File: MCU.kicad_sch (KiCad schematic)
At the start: 1 part, among them U5 STM32WB55CGUx

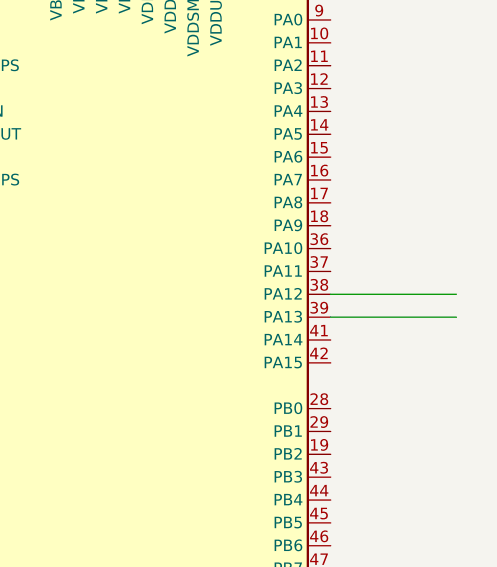
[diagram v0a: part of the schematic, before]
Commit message: added eink conn page
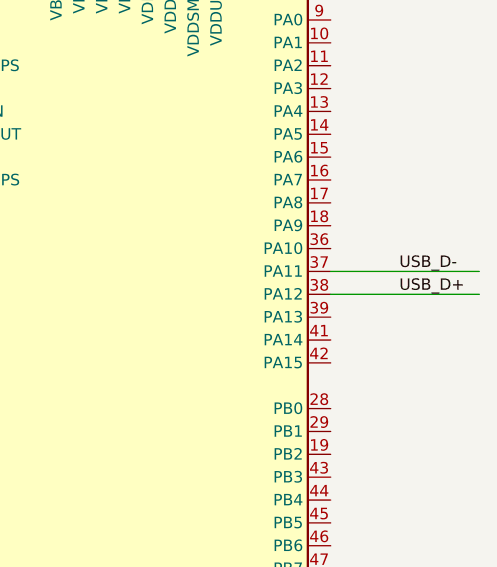
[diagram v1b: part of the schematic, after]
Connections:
- net USB_D-: now reaches U5.37 (PA11)
- net USB_D+: now reaches U5.38 (PA12)
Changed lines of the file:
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@@
+	(wire
+		(pts
+			(xy 168.91 87.63) (xy 185.42 87.63)
+		)
+		(stroke
+			(width 0)
+			(type default)
+		)
+	)
+	(wire
+		(pts
+			(xy 168.91 85.09) (xy 185.42 85.09)
+		)
+		(stroke
+			(width 0)
+			(type default)
+		)
+	)
 	(wire
 		(pts
@@
 	(wire
 		(pts
-			(xy 168.91 87.63) (xy 182.88 87.63)
-		)
-		(stroke
-			(width 0)
-			(type default)
-		)
-	)
-	(wire
-		(pts
 			(xy 146.05 137.16) (xy 146.05 139.7)
 		)
@@
 		)
 	)
-	(wire
-		(pts
-			(xy 168.91 90.17) (xy 182.88 90.17)
+	(label "USB_D-"
+		(at 176.53 85.09 0)
+		(effects
+			(font
+				(size 1.27 1.27)
+			)
+			(justify left bottom)
 		)
-		(stroke
-			(width 0)
-			(type default)
+	)
+	(label "USB_D+"
+		(at 176.53 87.63 0)
+		(effects
+			(font
+				(size 1.27 1.27)
+			)
+			(justify left bottom)
 		)
 	)
@@
 		(on_board yes)
 		(dnp no)
-		(fields_autoplaced yes)
 		(property "Reference" "U5"
 			(at 150.7333 130.81 0)

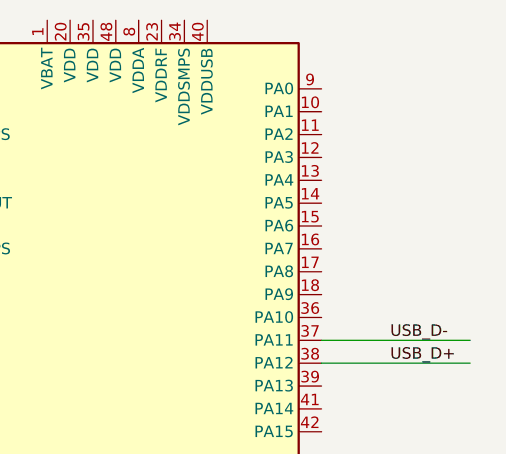
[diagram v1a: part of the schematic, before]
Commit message: eink-> mcu connections
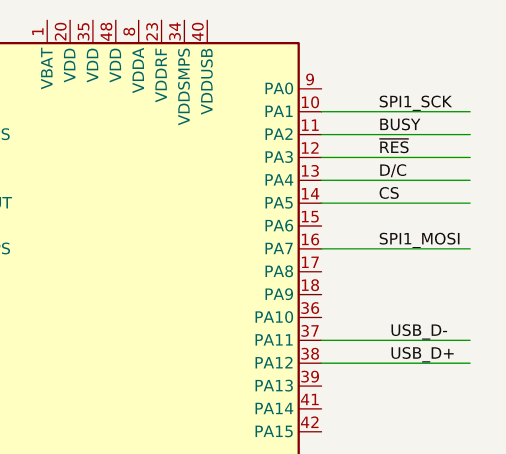
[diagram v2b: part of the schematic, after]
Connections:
- net SPI1_SCK: now reaches U5.10 (PA1)
- net BUSY: now reaches U5.11 (PA2)
- net ~{RES}: now reaches U5.12 (PA3)
- net D/C: now reaches U5.13 (PA4)
- net CS: now reaches U5.14 (PA5)
- net SPI1_MOSI: now reaches U5.16 (PA7)
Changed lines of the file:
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@@
+	(wire
+		(pts
+			(xy 168.91 64.77) (xy 185.42 64.77)
+		)
+		(stroke
+			(width 0)
+			(type default)
+		)
+	)
 	(wire
 		(pts
 			(xy 143.51 137.16) (xy 146.05 137.16)
+		)
+		(stroke
+			(width 0)
+			(type default)
+		)
+	)
+	(wire
+		(pts
+			(xy 168.91 69.85) (xy 185.42 69.85)
 		)
 		(stroke
@@
 	(wire
 		(pts
+			(xy 168.91 67.31) (xy 185.42 67.31)
+		)
+		(stroke
+			(width 0)
+			(type default)
+		)
+	)
+	(wire
+		(pts
 			(xy 143.51 130.81) (xy 143.51 137.16)
 		)
@@
 	(wire
 		(pts
+			(xy 168.91 62.23) (xy 185.42 62.23)
+		)
+		(stroke
+			(width 0)
+			(type default)
+		)
+	)
+	(wire
+		(pts
+			(xy 168.91 59.69) (xy 185.42 59.69)
+		)
+		(stroke
+			(width 0)
+			(type default)
+		)
+	)
+	(wire
+		(pts
 			(xy 146.05 137.16) (xy 148.59 137.16)
+		)
+		(stroke
+			(width 0)
+			(type default)
+		)
+	)
+	(wire
+		(pts
+			(xy 168.91 74.93) (xy 185.42 74.93)
 		)
 		(stroke
@@
 		)
 	)
+	(label "CS"
+		(at 175.26 69.85 0)
+		(effects
+			(font
+				(size 1.27 1.27)
+			)
+			(justify left bottom)
+		)
+	)
+	(label "D{slash}C"
+		(at 175.26 67.31 0)
+		(effects
+			(font
+				(size 1.27 1.27)
+			)
+			(justify left bottom)
+		)
+	)
+	(label "SPI1_MOSI"
+		(at 175.26 74.93 0)
+		(effects
+			(font
+				(size 1.27 1.27)
+			)
+			(justify left bottom)
+		)
+	)
 	(label "USB_D-"
 		(at 176.53 85.09 0)
+		(effects
+			(font
+				(size 1.27 1.27)
+			)
+			(justify left bottom)
+		)
+	)
+	(label "~{RES}"
+		(at 175.26 64.77 0)
 		(effects
 			(font
@@
 		(effects
 			(font
+				(size 1.27 1.27)
+			)
+			(justify left bottom)
+		)
+	)
+	(label "BUSY"
+		(at 175.26 62.23 0)
+		(effects
+			(font
+				(size 1.27 1.27)
+			)
+			(justify left bottom)
+		)
+	)
+	(label "SPI1_SCK"
+		(at 175.26 59.69 0)
+		(effects
+			(font

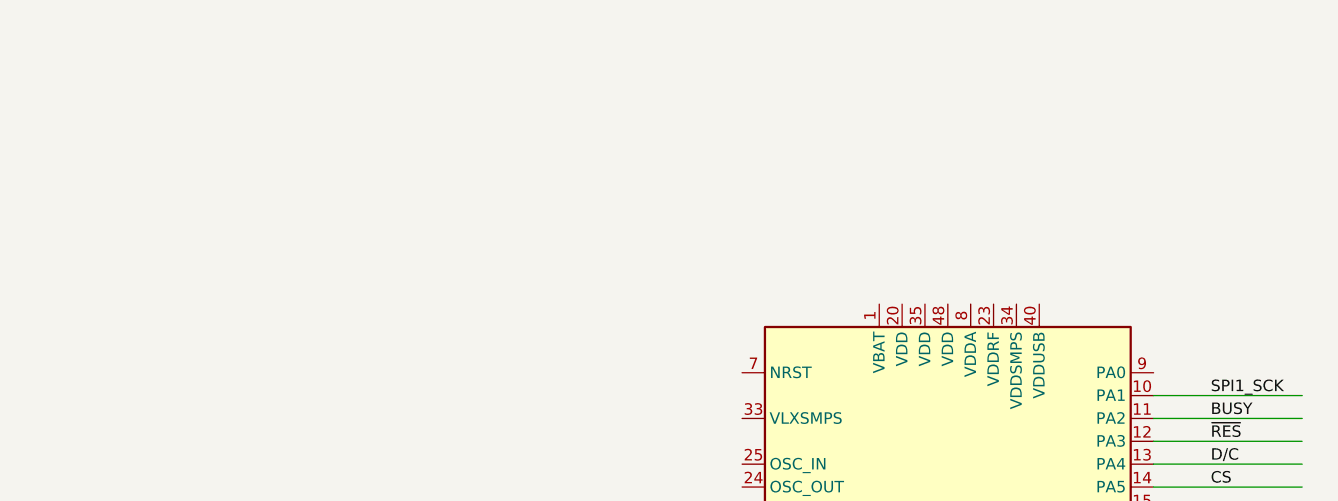
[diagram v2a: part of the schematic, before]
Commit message: added decoupling caps on mcu
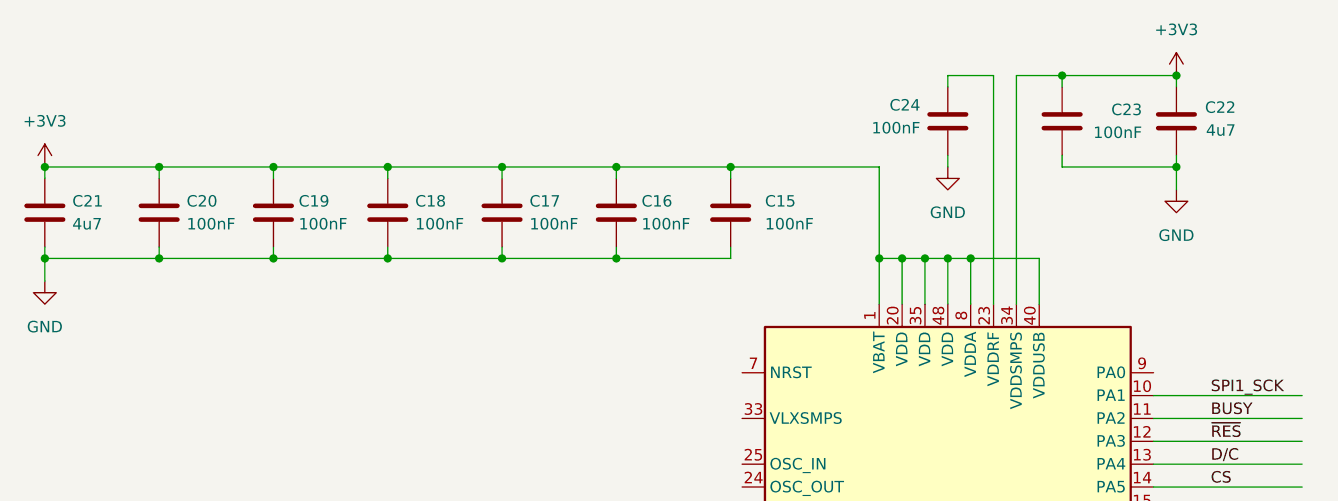
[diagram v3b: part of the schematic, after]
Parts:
- added C15, C16, C17, C18, C19, C20, C23, C24: 100nF, symbol Device:C
- added C21, C22: 4u7, symbol Device:C
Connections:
- net GND: now also C15.2, C16.2, C17.2, C18.2, C19.2, C20.2, C21.2, C22.2, C23.2, C24.2
- net +3V3: now reaches U5.1 (VBAT)
- net +3V3: now also U5.20 (VDD), U5.34 (VDDSMPS), U5.35 (VDD), U5.40 (VDDUSB), U5.48 (VDD), U5.8 (VDDA), C15.1, C16.1, C17.1, C18.1, C19.1, C20.1, C21.1, C22.1, C23.1
- net at U5.23 (VDDRF): now also C24.1

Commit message: generated pdf
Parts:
- added C25: 4u7, symbol Device:C
- added L1: 10uH, symbol Device:L
- added L3: 10nH, symbol Device:L
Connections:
- net GND: now also C25.2
- net SMPSFB: now reaches U5.31 (VFBSMPS)
- net SMPSFB: now also C25.1, L3.1
- net SMPSLX: now reaches U5.33 (VLXSMPS)
- net SMPSLX: now also L1.2
- new net SMPSLXL: L1.1, L3.2

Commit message: added externals crystal oscillators
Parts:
- added C26, C27: C, symbol Device:C
- added X1: 32MHz, symbol Device:Crystal_GND23_Small
- added X2: 32kHz768, symbol Device:Crystal_Small
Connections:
- net GND: now also C26.2, C27.2
- net LSE_IN: now reaches U5.2 (PC14)
- net LSE_IN: now also C26.1, X2.1
- net HSE_OUT: now reaches U5.24 (OSC_OUT)
- net HSE_OUT: now also X1.4
- net HSE_IN: now reaches U5.25 (OSC_IN)
- net HSE_IN: now also X1.1
- net LSE_OUT: now reaches U5.3 (PC15)
- net LSE_OUT: now also C27.1, X2.2
- net I2C_FUEL_GAUGE_CLK: now reaches U5.5 (PB8)
- net I2C_FUEL_GAUGE_IO: now reaches U5.6 (PB9)
- new net: X1.2 (G), X1.3 (G)

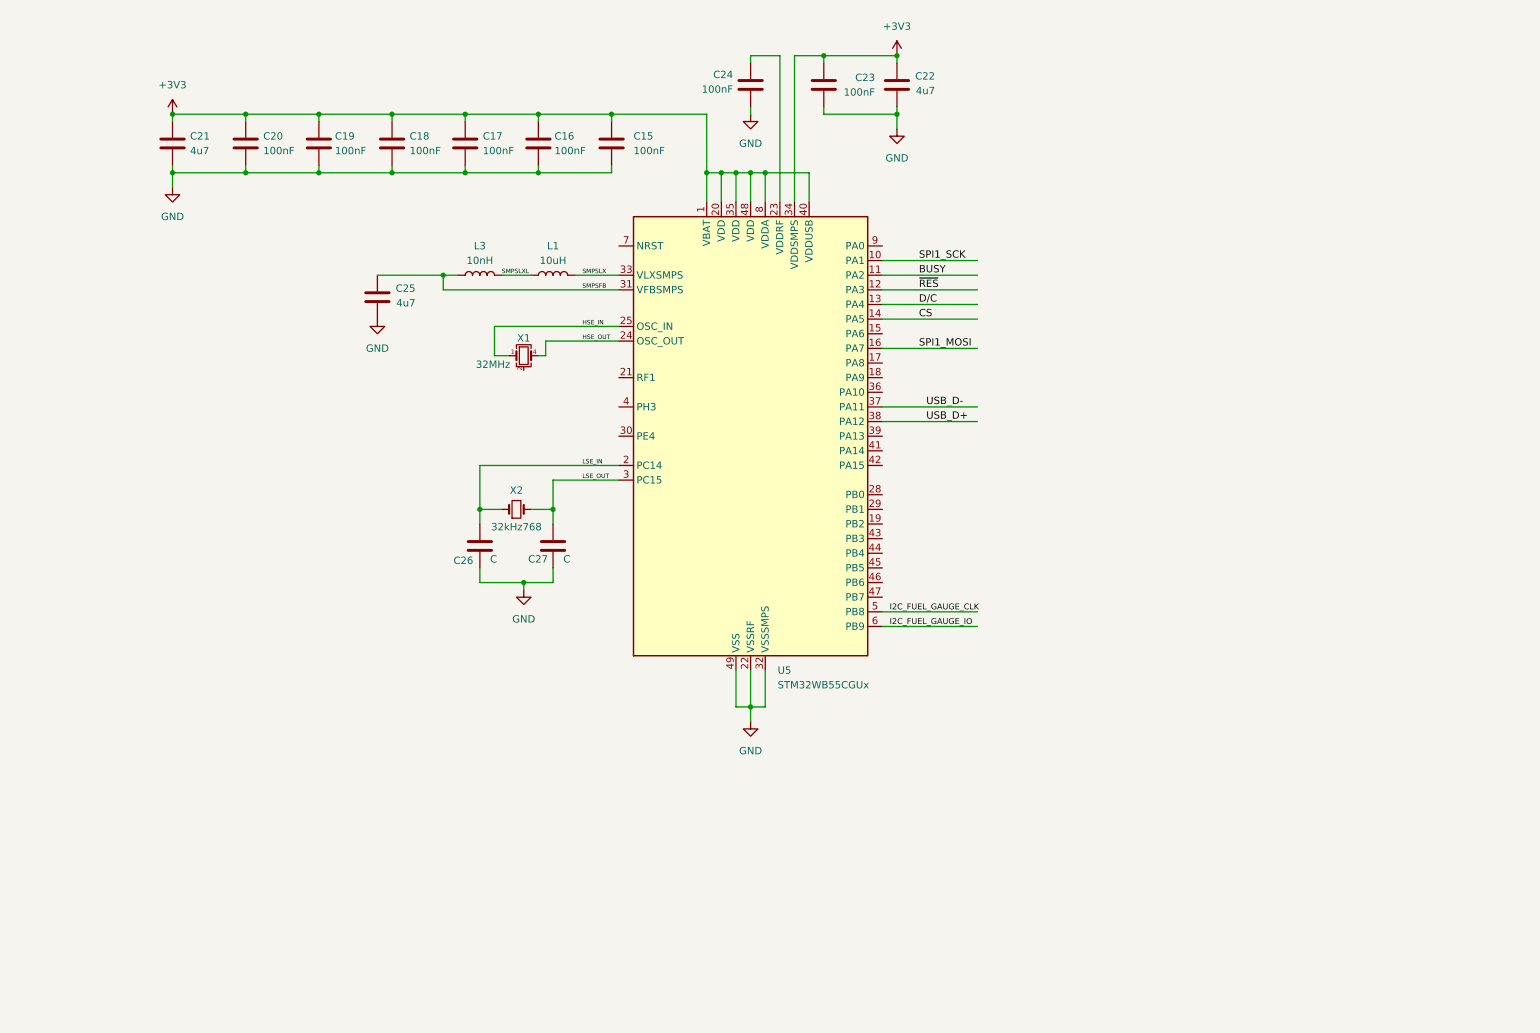
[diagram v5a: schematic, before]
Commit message: rf and debugger added
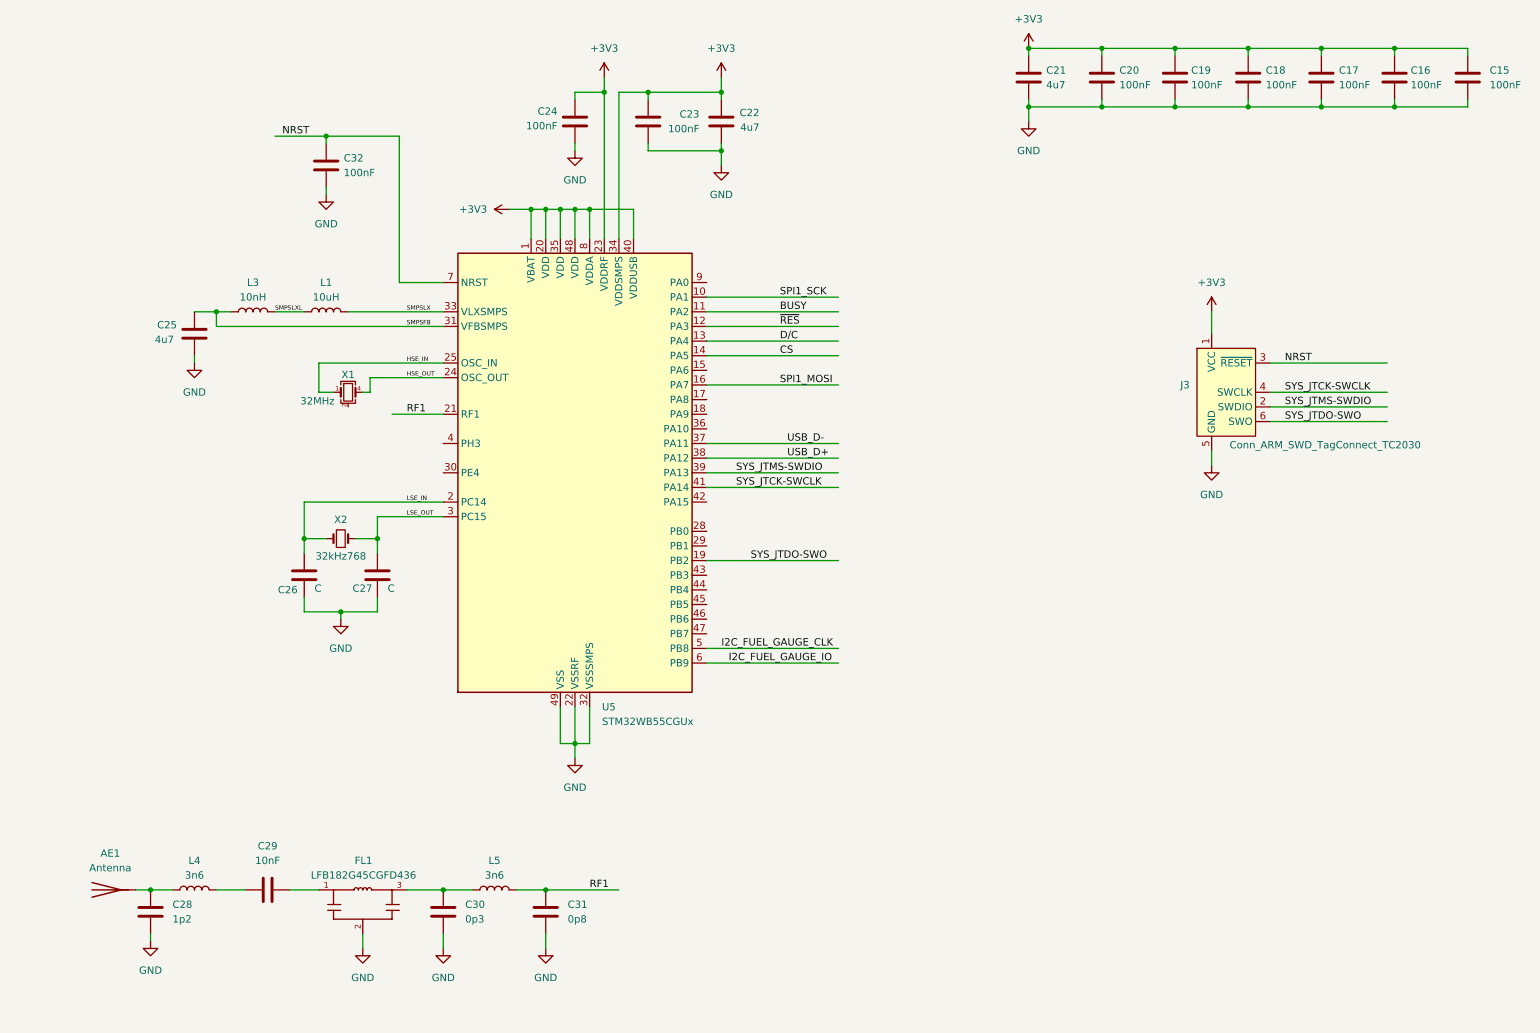
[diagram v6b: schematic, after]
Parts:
- added AE1: Antenna, symbol Device:Antenna
- added C28: 1p2, symbol Device:C
- added C29: 10nF, symbol Device:C
- added C30: 0p3, symbol Device:C
- added C31: 0p8, symbol Device:C
- added C32: 100nF, symbol Device:C
- added FL1: LFB182G45CGFD436, LFB182G45CGFD436:FIL_LFB182G45CGFD436, symbol LFB182G45CGFD436:LFB182G45CGFD436
- added J3: Conn_ARM_SWD_TagConnect_TC2030, Connector:Tag-Connect_TC2030-IDC-FP_2x03_P1.27mm_Vertical, symbol Connector:Conn_ARM_SWD_TagConnect_TC2030
- added L4, L5: 3n6, symbol Device:L
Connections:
- net +3V3: now also C24.1, U5.23 (VDDRF), J3.1 (VCC)
- net GND: now also C28.2, C30.2, C31.2, C32.2, FL1.2, FL1.2_1, J3.5 (GND)
- net SYS_JTDO-SWO: now reaches U5.19 (PB2)
- net SYS_JTDO-SWO: now also J3.6 (SWO)
- net RF1: now reaches U5.21 (RF1)
- net RF1: now also C31.1, L5.2
- net SYS_JTMS-SWDIO: now reaches U5.39 (PA13)
- net SYS_JTMS-SWDIO: now also J3.2 (SWDIO)
- net SYS_JTCK-SWCLK: now reaches U5.41 (PA14)
- net SYS_JTCK-SWCLK: now also J3.4 (SWCLK)
- net NRST: now reaches U5.7 (NRST)
- net NRST: now also C32.1, J3.3 (~{RESET})
- new net: C29.2, FL1.1
- new net: C30.1, FL1.3, L5.1
- new net: AE1.1 (A), C28.1, L4.1
- new net: C29.1, L4.2
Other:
- moved on the sheet: C15, C16, C17, C18, C19, C20, C21, C22, C23, C24, C25, C26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

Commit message: cleaned up rf & connected boot0
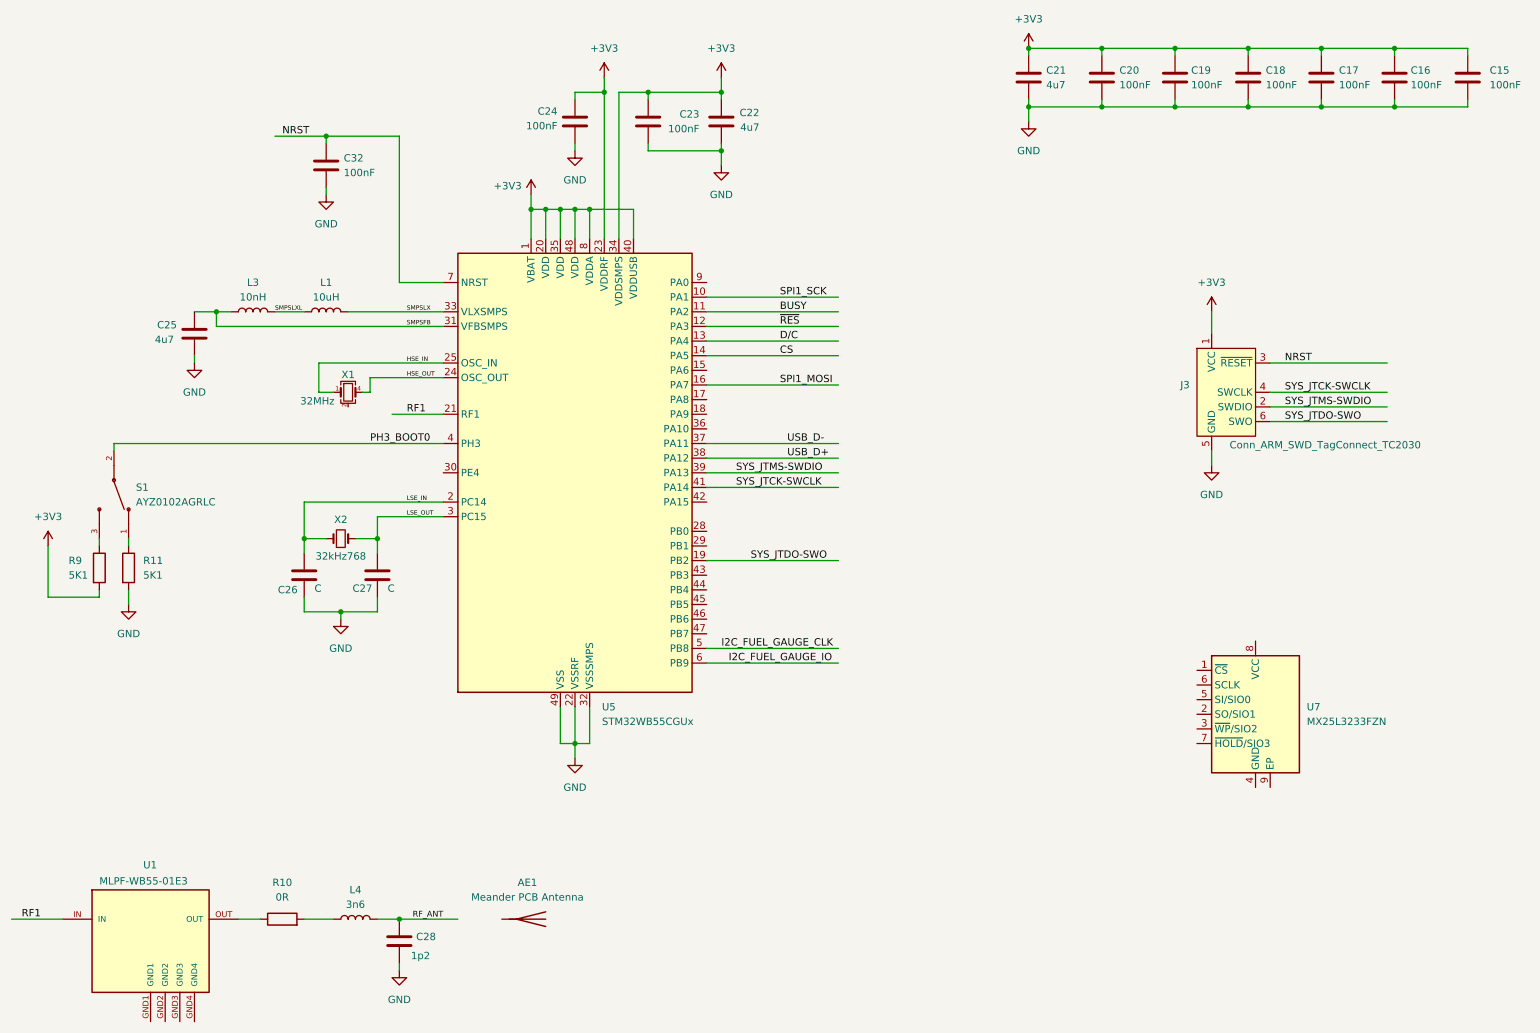
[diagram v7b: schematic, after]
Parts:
- removed C29: 10nF, symbol Device:C
- removed C30: 0p3, symbol Device:C
- removed C31: 0p8, symbol Device:C
- removed FL1: LFB182G45CGFD436, LFB182G45CGFD436:FIL_LFB182G45CGFD436, symbol LFB182G45CGFD436:LFB182G45CGFD436
- removed L5: 3n6, symbol Device:L
- added R10: 0R, symbol Device:R
- added R11, R9: 5K1, symbol Device:R
- added S1: AYZ0102AGRLC, AYZ0102AGRLC:SW_AYZ0102AGRLC, symbol AYZ0102AGRLC:AYZ0102AGRLC
- added U1: MLPF-WB55-01E3, MLPF-WB55-01E3:MLPF-WB55-01E3, symbol MLPF-WB55-01E3:MLPF-WB55-01E3
- added U7: MX25L3233FZN, Package_SON:WSON-8-1EP_6x5mm_P1.27mm_EP3.4x4mm, symbol Memory_Flash:MX25L3233FZN
- AE1: value Antenna -> Meander PCB Antenna
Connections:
- net +3V3: now also R9.2
- net GND: now also R11.2
- net RF1: now also U1.IN
- net RF_ANT: now reaches C28.1, L4.1
- net RF_ANT: no longer AE1.1 (A)
- net at L4.2: now also R10.2
- net PH3_BOOT0: now reaches U5.4 (PH3)
- net PH3_BOOT0: now also S1.2
- new net: R11.1, S1.1
- new net: R10.1, U1.OUT
- new net: R9.1, S1.3
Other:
- moved on the sheet: AE1, C28, L4
